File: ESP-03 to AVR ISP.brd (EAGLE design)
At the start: 21 x 26 mm, 17 parts, among them J1 AVR_SPI_PRG_62X3_LOCK, Q1 MOSFET-NCHANNELBSS138

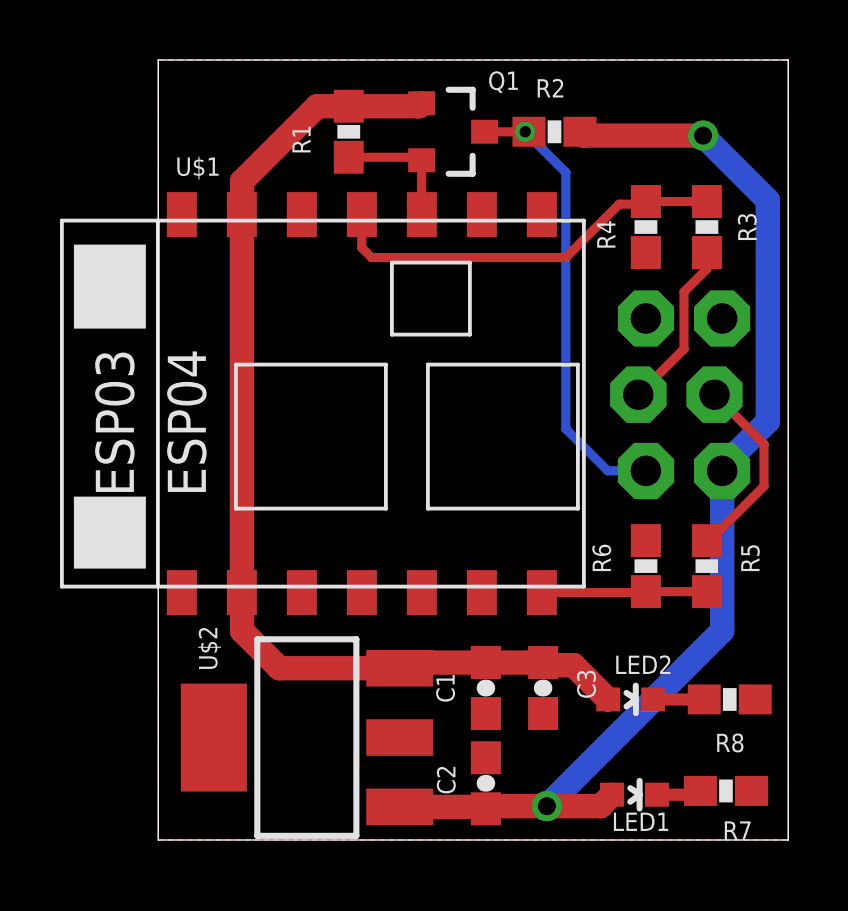
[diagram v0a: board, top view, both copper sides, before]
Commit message: PCB: Fixed wrong VCC connection. Removed Bootloader voltage divider. Changed LDO to 1117type
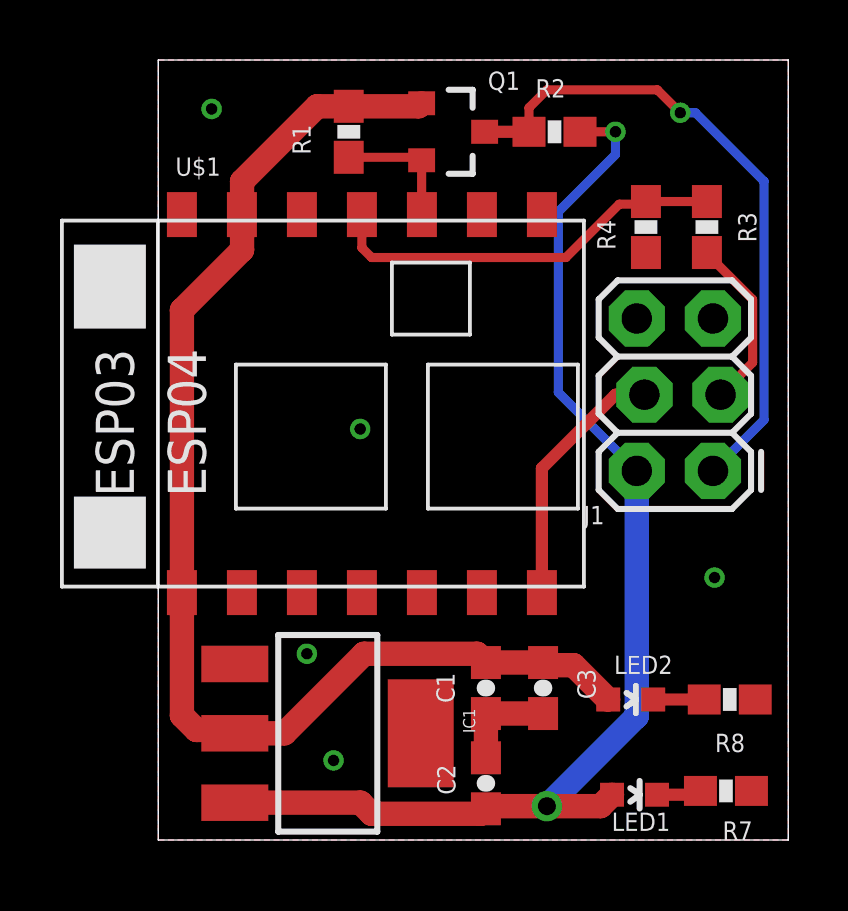
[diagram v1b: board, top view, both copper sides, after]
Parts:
- removed R5: 10k, SparkFun-Resistors:0603-RES
- removed R6: 20k, SparkFun-Resistors:0603-RES
- removed U$2: V_REG_MIC2920, SparkFun-PowerIC:SOT223
- added IC1: (no value), SparkFun-PowerIC:SOT223
- moved J1 2.23 mm to (18.5, 19.3), flipped to the top
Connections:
- removed net AVR_BOOT: J1.4, R5.1
- net 3.3V: now also IC1.2, U$1.VCC; no longer U$1.GPIO14, U$2.3
- net 5V: now also IC1.3; no longer U$2.1
- net BOOT: now also J1.4; no longer R5.2, R6.2
- net GND: now also IC1.1; no longer R6.1, U$2.2
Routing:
- net AVR_RX: track 15.2 -> 22.0 mm
- net 3.3V: track 35.4 -> 41.9 mm
- net AVR_BOOT: track 6.39 -> 0.00 mm
- net GND: track 0.00 -> 3.38 mm, vias 0 -> 5
- net BOOT: track 5.51 -> 8.58 mm
- net 5V: track 37.7 -> 39.9 mm
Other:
- board text added: "RX"
- board text added: "TX"
- board text removed: "AVR_RX"
- board text removed: "AVR_TX"

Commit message: Fixed PCB. Swithed to 1117 LDO.
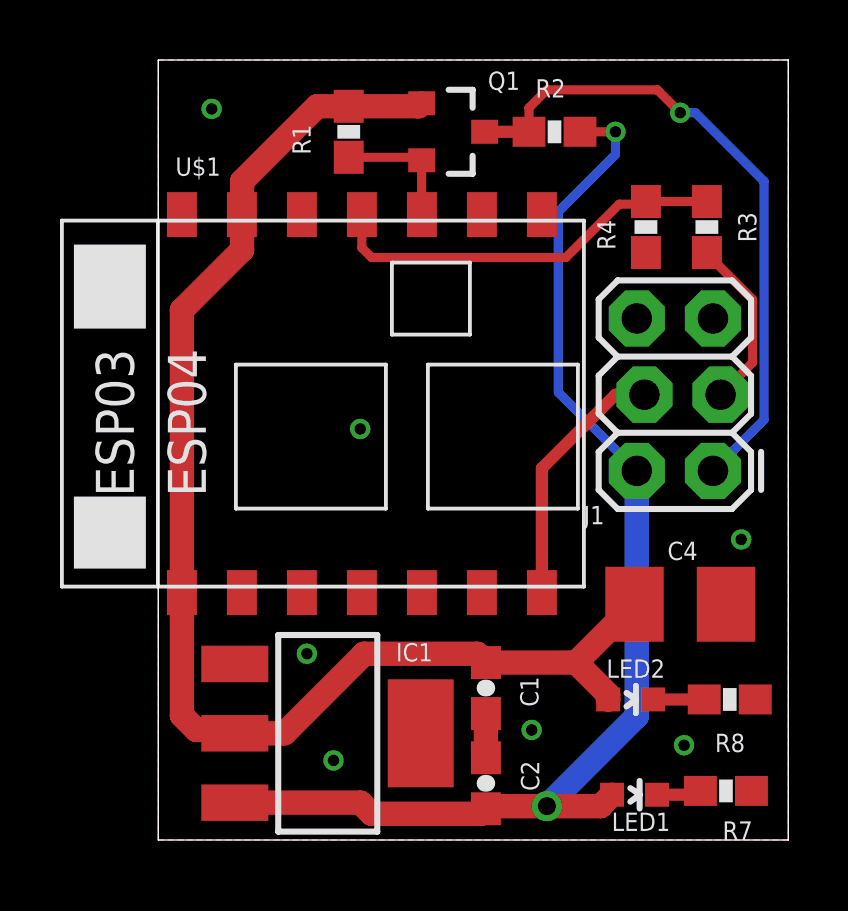
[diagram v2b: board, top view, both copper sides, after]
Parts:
- removed C3: 10uF, SparkFun-Capacitors:0603-CAP
- added C4: 100uF, rcl:B/3528-21R
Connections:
- net 3.3V: now also C4.+; no longer C3.1
- net GND: now also C4.-; no longer C3.2
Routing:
- net 3.3V: track 41.9 -> 44.8 mm
- net GND: track 3.38 -> 1.47 mm, vias 5 -> 7
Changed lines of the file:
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@@
 <elements>
 <element name="C1" library="SparkFun-Capacitors" package="0603-CAP" value="100nF" x="10.922" y="12.065" smashed="yes" rot="R270">
-<attribute name="NAME" x="9.271" y="12.573" size="0.6096" layer="25" font="vector" ratio="12" rot="R270"/>
+<attribute name="NAME" x="12.065" y="12.446" size="0.6096" layer="25" font="vector" ratio="12" rot="R270"/>
 </element>
 <element name="C2" library="SparkFun-Capacitors" package="0603-CAP" value="1uF" x="10.922" y="8.89" smashed="yes" rot="R90">
-<attribute name="NAME" x="9.906" y="8.509" size="0.6096" layer="25" font="vector" ratio="12" rot="R90"/>
+<attribute name="NAME" x="12.7" y="8.636" size="0.6096" layer="25" font="vector" ratio="12" rot="R90"/>
 </element>
 <element name="Q1" library="SparkFun-DiscreteSemi" package="SOT23-3" value="MOSFET-NCHANNELBSS138" x="9.779" y="30.607" smashed="yes" rot="R270">
@@
 <attribute name="NAME" x="14.172" y="17.526" size="0.6096" layer="25" ratio="12"/>
 </element>
-<element name="C3" library="SparkFun-Capacitors" package="0603-CAP" value="10uF" x="12.827" y="12.065" smashed="yes" rot="R270">
-<attribute name="NAME" x="13.97" y="12.7" size="0.6096" layer="25" font="vector" ratio="12" rot="R270"/>
-</element>
 <element name="R3" library="SparkFun-Resistors" package="0603-RES" value="10k" x="18.288" y="27.432" smashed="yes" rot="R90">
 <attribute name="NAME" x="19.939" y="26.924" size="0.6096" layer="25" font="vector" ratio="12" rot="R90"/>
@@
 </element>
 <element name="LED2" library="SparkFun-LED" package="LED-0603" value="3.3V" x="15.748" y="11.684" smashed="yes" rot="R270">
-<attribute name="NAME" x="17.145" y="13.1445" size="0.6096" layer="25" ratio="12" rot="R180"/>
+<attribute name="NAME" x="16.891" y="13.0175" size="0.6096" layer="25" ratio="12" rot="R180"/>
 <attribute name="VALUE" x="14.732" y="10.3505" size="0.8128" layer="27" ratio="12"/>
 </element>
@@
 <attribute name="NAME" x="19.558" y="10.541" size="0.6096" layer="25" font="vector" ratio="12" rot="R180"/>
 </element>
-<element name="IC1" library="SparkFun-PowerIC" package="SOT223" value="" x="5.65" y="10.556" rot="R270"/>
+<element name="IC1" library="SparkFun-PowerIC" package="SOT223" value="" x="5.65" y="10.556" smashed="yes" rot="R270">
+<attribute name="NAME" x="7.9225" y="12.9525" size="0.6096" layer="25" ratio="12"/>
+<attribute name="VALUE" x="5.4595" y="11.6355" size="0.4064" layer="27" rot="R270"/>
+</element>
+<element name="C4" library="rcl" package="B/3528-21R" value="100uF" x="17.399" y="14.859" smashed="yes" rot="R180">
+<attribute name="NAME" x="16.973" y="16.332" size="0.6096" layer="25" ratio="12"/>
+</element>
 </elements>
 <signals>
@@
 <contactref element="C1" pad="2"/>
 <contactref element="C2" pad="2"/>
-<contactref element="C3" pad="2"/>
 <contactref element="R4" pad="1"/>
 <contactref element="U$1" pad="GPIO15"/>
@@
 <contactref element="IC1" pad="1"/>
 <wire x1="10.922" y1="11.215" x2="10.922" y2="9.74" width="0.8128" layer="1"/>
-<wire x1="10.922" y1="11.215" x2="12.827" y2="11.215" width="0.8128" layer="1"/>
-<via x="18.542" y="15.748" extent="1-16" drill="0.381"/>
+<via x="19.431" y="17.018" extent="1-16" drill="0.381"/>
 <via x="5.842" y="9.652" extent="1-16" drill="0.381"/>
 <via x="1.778" y="31.369" extent="1-16" drill="0.381"/>
 <via x="6.731" y="20.701" extent="1-16" drill="0.381"/>
 <via x="4.953" y="13.208" extent="1-16" drill="0.381"/>
+<contactref element="C4" pad="-"/>
+<via x="17.526" y="10.16" extent="1-16" drill="0.381"/>
+<via x="12.446" y="10.668" extent="1-16" drill="0.381"/>
 </signal>
 <signal name="ES_TX">
@@
 <contactref element="Q1" pad="1"/>
 <contactref element="R1" pad="2"/>
-<contactref element="C3" pad="1"/>
 <contactref element="U$1" pad="CH_PD"/>
 <contactref element="LED2" pad="A"/>
@@
 <wire x1="8.679" y1="31.457" x2="8.779" y2="31.557" width="0.8128" layer="1"/>
 <wire x1="14.998" y1="11.684" x2="14.986" y2="11.684" width="0.8128" layer="1"/>
-<wire x1="14.986" y1="11.684" x2="13.843" y2="12.827" width="0.8128" layer="1"/>
-<wire x1="13.843" y1="12.827" x2="12.915" y2="12.827" width="0.8128" layer="1"/>
-<wire x1="12.915" y1="12.827" x2="12.827" y2="12.915" width="0.8128" layer="1"/>
-<wire x1="12.827" y1="12.915" x2="10.922" y2="12.915" width="0.8128" layer="1"/>
 <contactref element="IC1" pad="2"/>
 <contactref element="U$1" pad="VCC"/>
@@
 <wire x1="6.858" y1="13.208" x2="10.629" y2="13.208" width="0.8128" layer="1"/>
 <wire x1="10.629" y1="13.208" x2="10.922" y2="12.915" width="0.8128" layer="1"/>
+<contactref element="C4" pad="+"/>
+<wire x1="10.922" y1="12.915" x2="13.93" y2="12.915" width="0.8128" layer="1"/>
+<wire x1="13.93" y1="12.915" x2="15.874" y2="14.859" width="0.8128" layer="1"/>
+<wire x1="14.998" y1="11.684" x2="14.998" y2="11.847" width="0.8128" layer="1"/>
+<wire x1="14.998" y1="11.847" x2="13.93" y2="12.915" width="0.8128" layer="1"/>
 </signal>
 <signal name="5V">
